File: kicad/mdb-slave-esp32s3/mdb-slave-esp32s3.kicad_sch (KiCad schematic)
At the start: 39 parts, among them J2 MDB_Connector, J3 Conn_02x11_Odd_Even, P2 USB_C_Plug_USB2.0, SW1 SW_Push, SW3 SW_Push, U2 TS1117B, U3 ESP32-S3FH4R2, U4 PC817, U5 PC817, Y2 40000hz

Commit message: Refacting kicad pcb
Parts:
- removed AE2: Antenna, RF_Antenna:Texas_SWRA117D_2.4GHz_Right, symbol Device:Antenna
- removed C10, C11: 22pf, Capacitor_SMD:C_0603_1608Metric, symbol Device:C
- removed C12, C13, C14: C, Capacitor_SMD:C_0603_1608Metric, symbol Device:C
- removed C7: 22uf, Capacitor_Tantalum_SMD:CP_EIA-3216-18_Kemet-A, symbol Device:C_Polarized
- removed C8: 1.8pf, Capacitor_SMD:C_0603_1608Metric, symbol Device:C
- removed D3: 1N5819HWQ, Diode_SMD:D_SOD-123, symbol Device:D
- removed D6, D7: LED, LED_SMD:LED_0603_1608Metric, symbol Device:LED
- removed J2: MDB_Connector, Connector_Molex:Molex_Mini-Fit_Jr_5566-06A_2x03_P4.20mm_Vertical, symbol Connector_Generic:Conn_02x03_Top_Bottom
- removed L2: 2.4nh, Inductor_SMD:L_0603_1608Metric, symbol Device:L
- removed P2: USB_C_Plug_USB2.0, Connector_USB:USB_C_Receptacle_G-Switch_GT-USB-7010ASV, symbol Connector:USB_C_Plug_USB2.0
- removed R12, R15, R16, R17, R18, R19, R20, R24: 3.3k, Resistor_SMD:R_0603_1608Metric, symbol Device:R
- removed R13: 180ohm, Resistor_SMD:R_0603_1608Metric, symbol Device:R
- removed R14, R22, R23: 240ohm, Resistor_SMD:R_0603_1608Metric, symbol Device:R
- removed SW3: SW_Push, Button_Switch_SMD:SW_Tactile_SPST_NO_Straight_CK_PTS636Sx25SMTRLFS, symbol Switch:SW_Push
- removed TP2, TP3: TestPoint, TestPoint:TestPoint_Pad_D1.0mm, symbol Connector:TestPoint
- removed U2: TS1117B, Package_TO_SOT_SMD:SOT-223-3_TabPin2, symbol Regulator_Linear:LM317_SOT-223
- removed U4, U5: PC817, Package_DIP:DIP-4_W7.62mm, symbol Isolator:PC817
- removed Y2: 40000hz, Crystal:Crystal_HC49-4H_Vertical, symbol Device:Crystal
- added AE1: Antenna, RF_Antenna:Texas_SWRA117D_2.4GHz_Left, symbol Device:Antenna
- added C1, C2: C, Capacitor_SMD:C_0603_1608Metric, symbol Device:C
- added C4: 1.8pf, Capacitor_SMD:C_0603_1608Metric, symbol Device:C
- added C5, C6, C7: 22pf, Capacitor_SMD:C_0603_1608Metric, symbol Device:C
- added D1: 1N5819HWQ, Diode_SMD:D_SOD-123, symbol Device:D
- added D2, D3: LED, LED_SMD:LED_0603_1608Metric, symbol Device:LED
- added J1: MDB_Connector, Connector_Molex:Molex_Mini-Fit_Jr_5566-06A_2x03_P4.20mm_Vertical, symbol Connector_Generic:Conn_02x03_Top_Bottom
- added J2: USB_C_Receptacle_USB2.0_16P, Connector_USB:USB_C_Receptacle_G-Switch_GT-USB-7010ASV, symbol Connector:USB_C_Receptacle_USB2.0_16P
- added L1: 2.4nh, Inductor_SMD:L_0603_1608Metric, symbol Device:L
- added R1, R3, R4, R6, R7, R9: 3.3k, Resistor_SMD:R_0603_1608Metric, symbol Device:R
- added R10: 240ohm, Resistor_SMD:R_0603_1608Metric, symbol Device:R
- added R2, R5: 180ohm, Resistor_SMD:R_0603_1608Metric, symbol Device:R
- added U1, U2: PC817, Package_DIP:DIP-4_W7.62mm, symbol Isolator:PC817
- added U4: AMS1117-3.3, Package_TO_SOT_SMD:SOT-223, symbol Regulator_Linear:AMS1117-3.3
- added Y1: 40000hz, Crystal:Crystal_HC49-4H_Vertical, symbol Device:Crystal
- R11: value 180ohm -> 240ohm
- R8: value 390ohm -> 3.3k
- U3: value ESP32-S3FH4R2 -> ESP32-S3R8
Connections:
- net +3V3: now also J3.18 (Pin_18), R11.2, C1.2, C2.2, C7.2, R1.2, R3.1, R4.2, R5.1, U4.2 (VO); no longer J3.16 (Pin_16), TP1.1
- net GND: now also C1.1, C2.1, C5.1, C6.1, C7.1, D2.1 (K), D3.1 (K), J1.2 (Pin_2), J2.A1 (GND), J2.A12 (GND), J2.B1 (GND), J2.B12 (GND), J2.S1 (SHIELD), L1.2, R6.2, R7.2, R9.2, U1.3, U4.1 (GND); no longer J3.1 (Pin_1), J3.18 (Pin_18)
- net boot: now also J3.16 (Pin_16), R4.1
- net io1: now also J3.5 (Pin_5); no longer J3.7 (Pin_7)
- net io17: now also J3.17 (Pin_17); no longer J3.19 (Pin_19)
- net io18: now also J3.19 (Pin_19); no longer J3.21 (Pin_21)
- net io2: now also J3.7 (Pin_7); no longer J3.9 (Pin_9)
- net io21: now also J3.21 (Pin_21), R10.2
- net io4: now also J3.9 (Pin_9), R1.1, U1.4; no longer J3.11 (Pin_11)
- net io5: now also J3.11 (Pin_11), U2.2; no longer J3.13 (Pin_13)
- net io6: now also J3.13 (Pin_13); no longer J3.15 (Pin_15)
- net io7: now also J3.15 (Pin_15); no longer J3.17 (Pin_17)
- net mdb_communications_common: now also J1.6 (Pin_6), U1.2, U2.3
- net mdb_master_receive: now also J1.4 (Pin_4), U2.4
- net mdb_master_transmit: now also J1.5 (Pin_5), R2.1; no longer R11.1
- net u0rxd: now also J3.3 (Pin_3); no longer J3.5 (Pin_5)
- net u0txd: now also J3.1 (Pin_1); no longer J3.3 (Pin_3)
- net usb+: now also J2.A6 (D+), J2.B6 (D+)
- net usb-: now also J2.A7 (D-), J2.B7 (D-)
- net vin: now also D1.1 (K), J1.1 (Pin_1), U4.3 (VI)
- net at U3.52 (GPIO46): now also R9.1
- net at U3.53 (XTAL_N): now also C5.2, Y1.2
- net at U3.1 (LNA_IN/RF): now also C4.2
- net vdd_spi: now reaches U3.29 (VDD_SPI)
- net spihd: now reaches U3.30 (SPIHD/GPIO27)
- net spiwp: now reaches U3.31 (SPIWP/GPIO28)
- net spics0: now reaches U3.32 (SPICS0/GPIO29)
- net spiclk: now reaches U3.33 (SPICLK/GPIO30)
- net spiq: now reaches U3.34 (SPIQ/GPIO31)
- net spid: now reaches U3.35 (SPID/GPIO32)
- net at U3.4 (CHIP_PU/RESET): now also TP1.1, R3.2
- net at U3.51 (GPIO45): now also R6.1
- net at U3.54 (XTAL_P): now also C6.2, Y1.1
- net at R8.1: now also J2.A5 (CC1)
- new net: D1.2 (A), J2.A4 (VBUS), J2.A9 (VBUS), J2.B4 (VBUS), J2.B9 (VBUS)
- new net: R5.2, U2.1
- new net: R2.2, U1.1
- new net: J2.B5 (CC2), R7.1
- new net: D3.2 (A), R11.1
- new net: D2.2 (A), R10.1
- new net: AE1.1 (A), C4.1, L1.1
- no-connect marks 24 -> 26

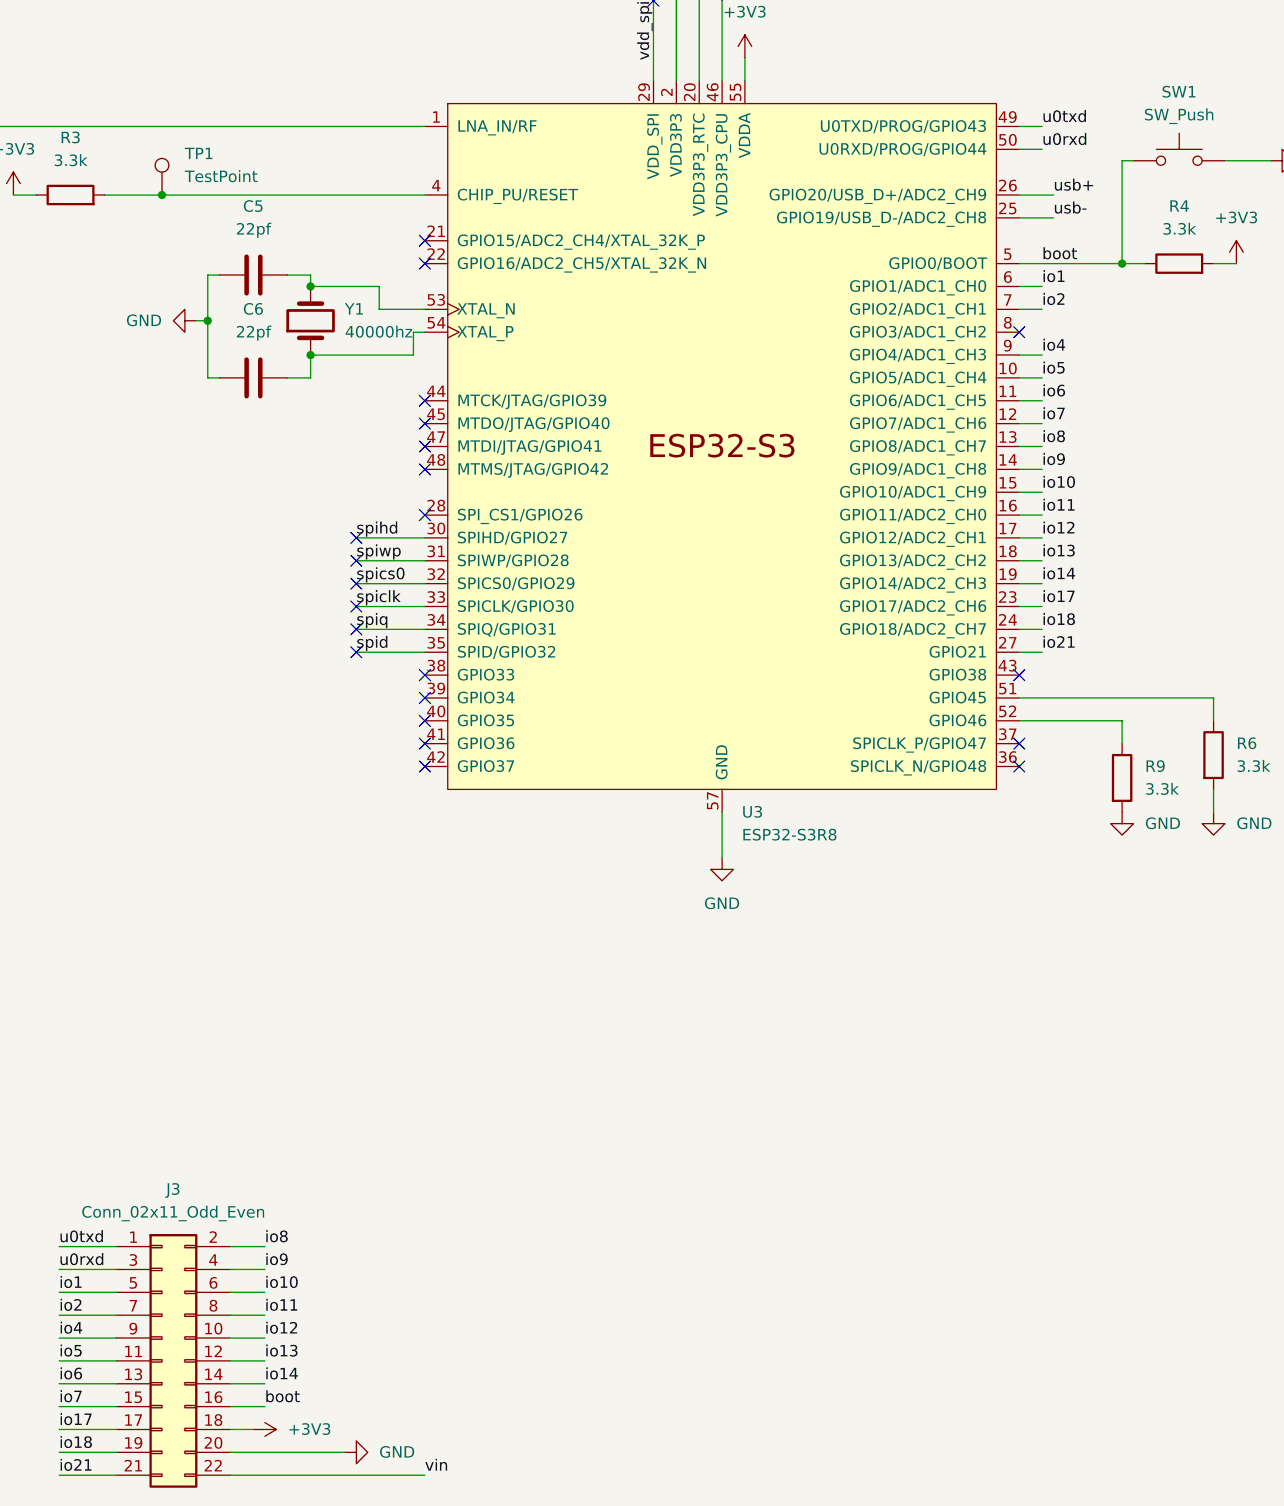
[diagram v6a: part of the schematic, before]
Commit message: Refacting Kicad layout
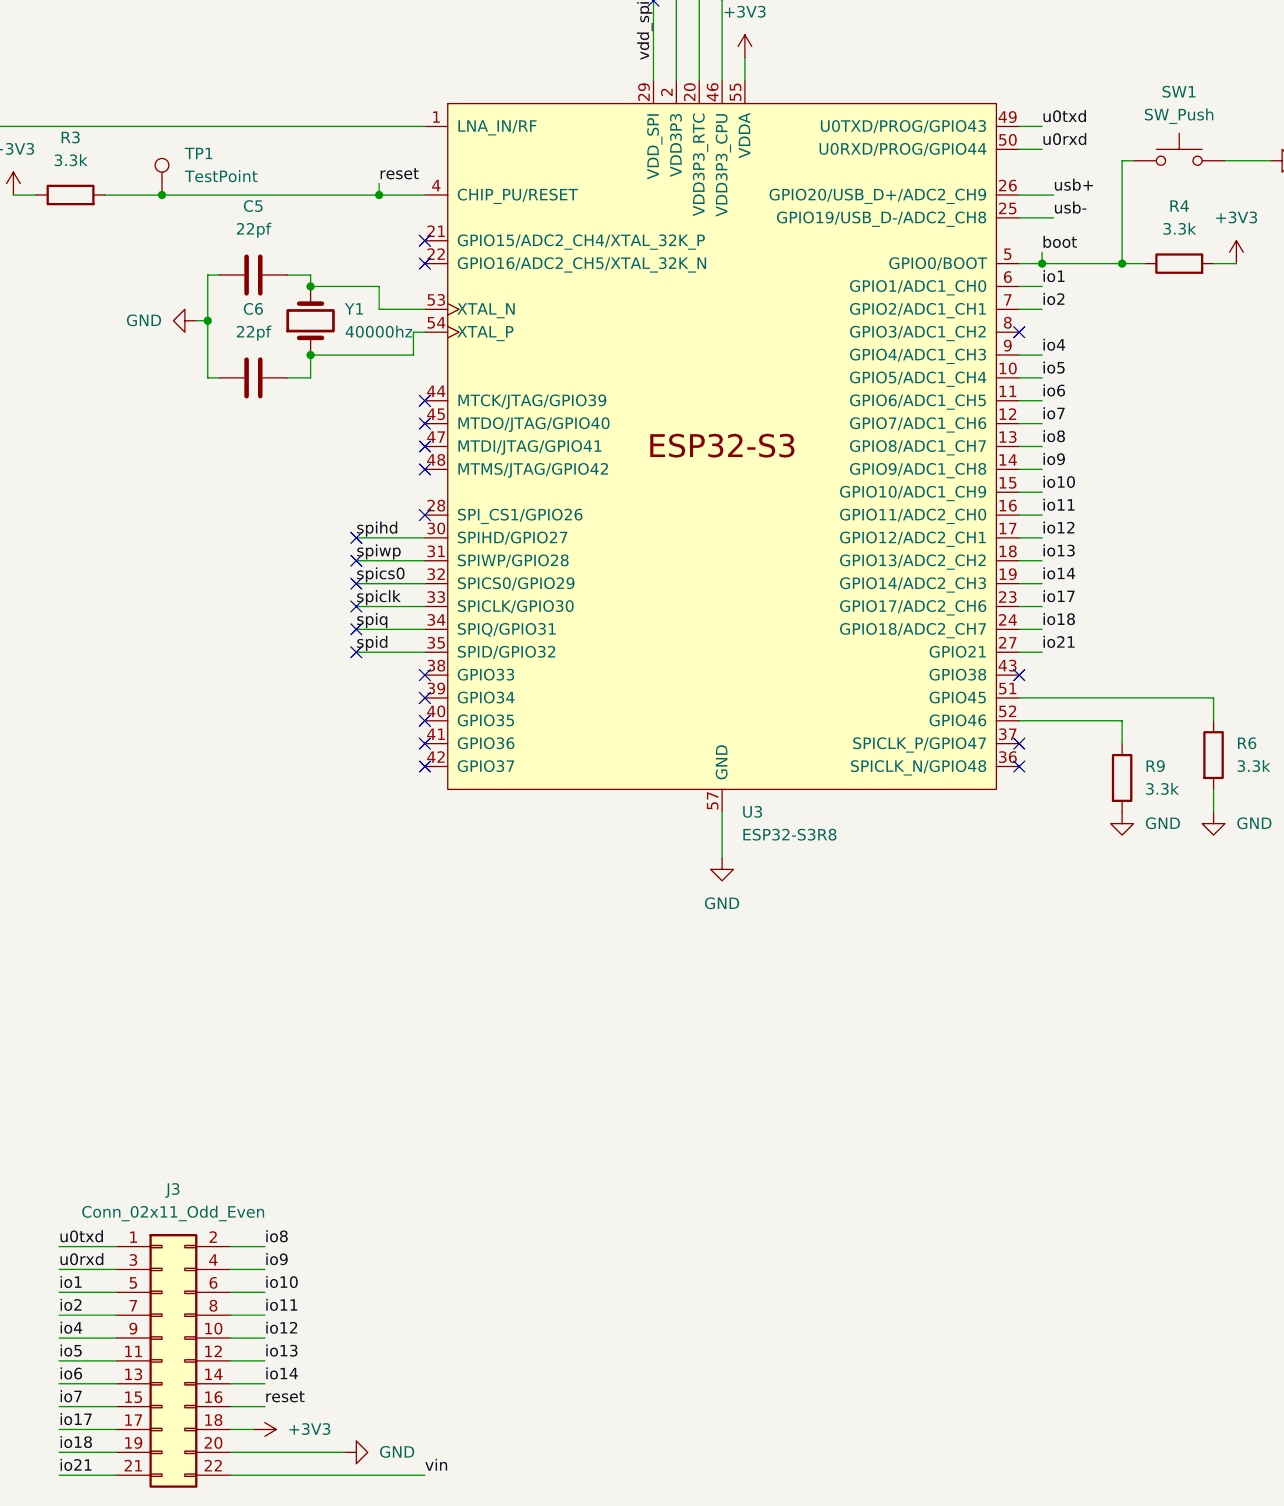
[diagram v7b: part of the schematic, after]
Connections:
- net boot: no longer J3.16 (Pin_16)
- net reset: now reaches R3.2, TP1.1, U3.4 (CHIP_PU/RESET)
- net reset: now also J3.16 (Pin_16)
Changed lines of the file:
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@@
+	)
+	(junction
+		(at 160.02 114.3)
+		(diameter 0)
+		(color 0 0 0 0)
+	)
+	(junction
+		(at 86.36 106.68)
+		(diameter 0)
+		(color 0 0 0 0)
 	)
 	(junction
@@
 	(wire
 		(pts
-			(xy 62.23 106.68) (xy 91.44 106.68)
+			(xy 62.23 106.68) (xy 86.36 106.68)
 		)
 		(stroke
@@
 	(wire
 		(pts
-			(xy 157.48 114.3) (xy 168.91 114.3)
+			(xy 157.48 114.3) (xy 160.02 114.3)
+		)
+		(stroke
+			(width 0)
+			(type default)
+		)
+	)
+	(wire
+		(pts
+			(xy 160.02 113.03) (xy 160.02 114.3)
 		)
 		(stroke
@@
 	(wire
 		(pts
+			(xy 86.36 106.68) (xy 91.44 106.68)
+		)
+		(stroke
+			(width 0)
+			(type default)
+		)
+	)
+	(wire
+		(pts
 			(xy 50.8 238.76) (xy 57.15 238.76)
 		)
@@
 	(wire
 		(pts
+			(xy 160.02 114.3) (xy 168.91 114.3)
+		)
+		(stroke
+			(width 0)
+			(type default)
+		)
+	)
+	(wire
+		(pts
 			(xy 50.8 246.38) (xy 57.15 246.38)
 		)
@@
 		(pts
 			(xy 83.82 149.86) (xy 91.44 149.86)
+		)
+		(stroke
+			(width 0)
+			(type default)
+		)
+	)
+	(wire
+		(pts
+			(xy 86.36 105.41) (xy 86.36 106.68)
 		)
 		(stroke
@@
 		)
 	)
+	(label "reset"
+		(at 86.36 105.41 0)
+		(fields_autoplaced yes)
+		(effects
+			(font
+				(size 1.27 1.27)
+			)
+			(justify left bottom)
+		)
+	)
 	(label "io18"
 		(at 50.8 246.38 0)
@@
 		)
 	)
-	(label "boot"
+	(label "reset"
 		(at 73.66 241.3 0)
 		(fields_autoplaced yes)
@@
 	)
 	(label "boot"
-		(at 160.02 114.3 0)
+		(at 160.02 113.03 0)
 		(fields_autoplaced yes)
 		(effects

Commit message: Refacting PCB
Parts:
- removed TP1: TestPoint, TestPoint:TestPoint_Pad_D1.0mm, symbol Connector:TestPoint
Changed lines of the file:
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@@
 		(color 0 0 0 0)
 	)
-	(junction
-		(at 62.23 106.68)
-		(diameter 0)
-		(color 0 0 0 0)
-	)
 	(no_connect
 		(at 231.14 185.42)
@@
 	(wire
 		(pts
-			(xy 62.23 106.68) (xy 86.36 106.68)
+			(xy 55.88 106.68) (xy 86.36 106.68)
 		)
 		(stroke
@@
 		(pts
 			(xy 86.36 105.41) (xy 86.36 106.68)
-		)
-		(stroke
-			(width 0)
-			(type default)
-		)
-	)
-	(wire
-		(pts
-			(xy 55.88 106.68) (xy 62.23 106.68)
 		)
 		(stroke
@@
 					(unit 1)
 				)
-			)
-		)
-	)
-	(symbol
-		(lib_id "Connector:TestPoint")
-		(at 62.23 106.68 0)
-		(unit 1)
-		(exclude_from_sim no)
-		(in_bom yes)
-		(on_board yes)
-		(dnp no)
-		(fields_autoplaced yes)
-		(property "Reference" "TP1"
-			(at 64.77 102.1079 0)
-			(effects
-				(font
-					(size 1.27 1.27)
-				)
-				(justify left)
-			)
-		)
-		(property "Value" "TestPoint"
-			(at 64.77 104.6479 0)
-			(effects
-				(font
-					(size 1.27 1.27)
-				)
-				(justify left)
-			)
-		)
-		(property "Footprint" "TestPoint:TestPoint_Pad_D1.0mm"
-			(at 67.31 106.68 0)
-			(effects
-				(font
-					(size 1.27 1.27)
-				)
-				(hide yes)
-			)
-		)
-		(property "Datasheet" "~"
-			(at 67.31 106.68 0)
-			(effects
-				(font
-					(size 1.27 1.27)
-				)
-				(hide yes)
-			)
-		)
-		(property "Description" "test point"
-			(at 62.23 106.68 0)
-			(effects
-				(font
-					(size 1.27 1.27)
-				)
-				(hide yes)
-			)
-		)
-		(pin "1"
-		)
-		(instances
-			(project "mdb-slave-esp32s3"
-				(path "/95980b25-0707-441d-ba83-7f6c6e1d1aaa"
-					(reference "TP1")
-					(unit 1)
-				)
